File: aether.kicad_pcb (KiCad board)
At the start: 4 copper layers, 87 x 69.8 mm, 83 parts, among them J1 USB_C_Receptacle_USB2.0, J2 Conn_02x12_Top_Bottom, U1 CP2102N, U2 MCP73871_U, U3 LP2985-3.3, U4 LTC3525-5, U5 LoRa-E5

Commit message: Generated more 3d models for pcb
-
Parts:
- AE1: footprint Connector_Coaxial:SMA_Amphenol_132289_EdgeMount -> Connector_Coaxial:SMA_Amphenol_132134_Vertical
- J1: footprint Connector_USB:USB_C_Receptacle_Amphenol_12401610E4-2A -> Connector_USB:USB_C_Receptacle_XKB_U262-16XN-4BVC11
- moved Battery_Connect1 1.75 mm to (131.9, 136.0), turned to 180 degrees
- moved AE1 0.35 mm to (186.1, 94.0), turned to 90 degrees

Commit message: PCB edits
-
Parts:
- J2: value Conn_02x12_Top_Bottom -> Conn_01x05; footprint Connector_PinHeader_2.54mm:PinHeader_2x12_P2.54mm_Vertical -> Connector_PinHeader_1.27mm:PinHeader_1x05_P1.27mm_Vertical
- moved PMSensor1 49.9 mm to (184.8, 121.9), turned to -90 degrees
- moved R23 42.0 mm to (177.5, 123.8)
- moved R22 42.0 mm to (172.7, 123.8)
- moved J2 13.3 mm to (185.4, 91.4)
- moved AE1 13.1 mm to (182.9, 106.7)
- moved S1 12.3 mm to (174.6, 76.2)
- moved C14 12.0 mm to (153.9, 89.5)
- moved R21 6.87 mm to (148.6, 89.5)
- moved R20 6.79 mm to (148.6, 85.7)
- moved R19 6.06 mm to (154.0, 85.7)
- moved C2 4.45 mm to (123.2, 94.0)
- moved D1 4.44 mm to (122.6, 80.6)
- moved DC_InputTest1 4.44 mm to (121.9, 87.6)
- moved H3 3.42 mm to (184.8, 74.9)
- moved H1 3.18 mm to (184.8, 138.4)
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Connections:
- J2 pad 1: USB5V -> PA13/SWDIO
- J2 pad 2: +3.3V -> PA14/SWCLK
- J2 pad 3: PA13/SWDIO -> GND
- J2 pad 4: PA14/SWCLK -> RST
- J2 pad 5: RST -> unconnected-(J2-Pad5)
- U5 pad 24: PA13/SCK -> PB13/SCK
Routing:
- net GND: track 0.00 -> 2.19 mm
- net Net-(R15-Pad2): track 0.00 -> 0.97 mm
- added copper zone on In1.Cu, net +3.3V
- added copper zone on In2.Cu, net GND
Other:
- board size 87 x 69.8 mm -> 83.8 x 68.6 mm

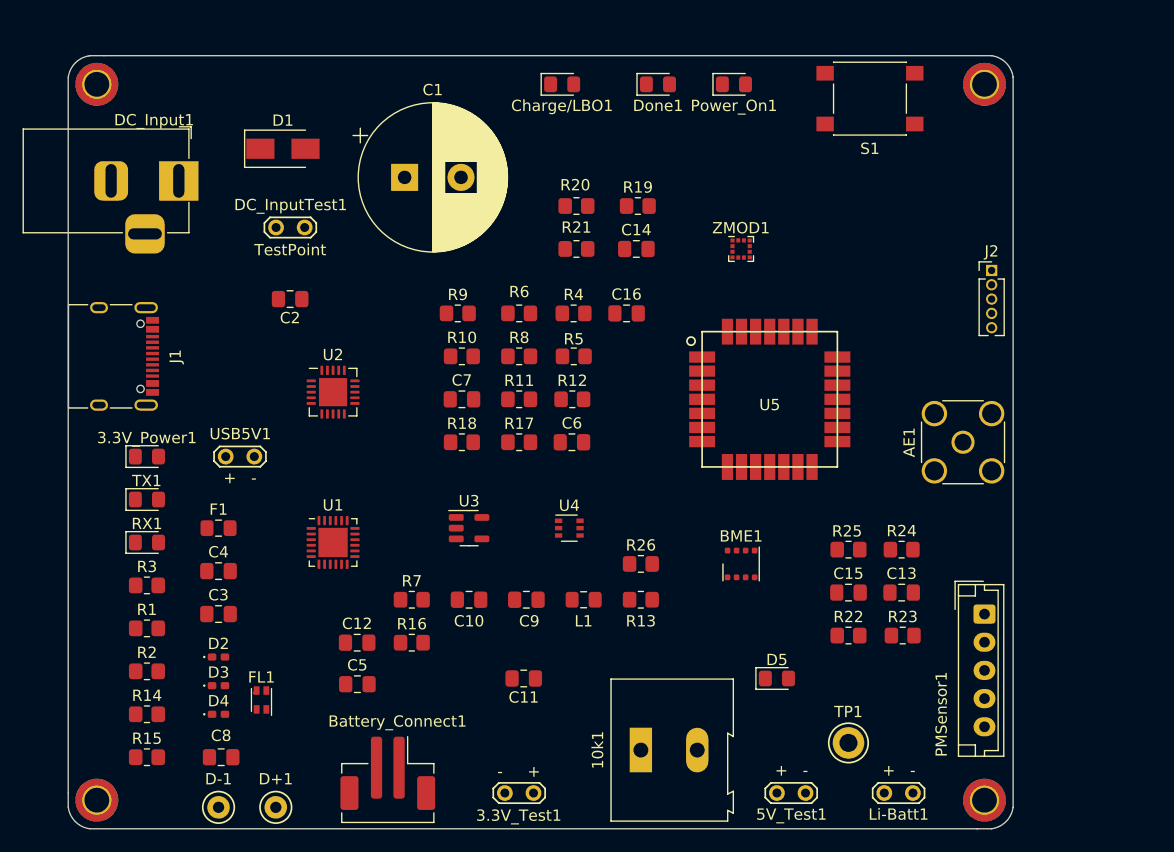
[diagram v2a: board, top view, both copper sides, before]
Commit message: Rearranged PCB for more efficient routing
-
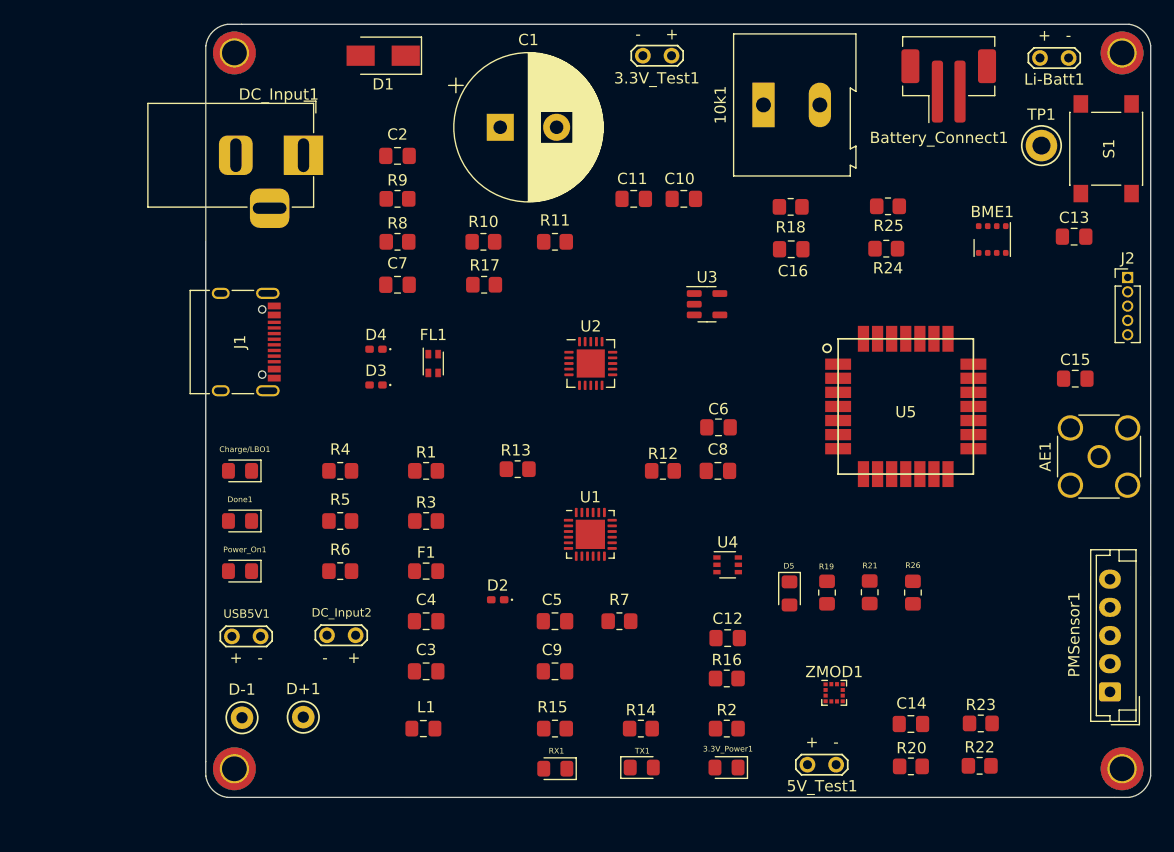
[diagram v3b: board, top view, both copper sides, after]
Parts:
- DC_Input2: renamed from DC_InputTest1; value TestPoint -> - +
- moved Battery_Connect1 78.7 mm to (181.6, 75.1), turned to 0 degrees
- moved Li-Batt1 66.6 mm to (189.7, 72.6)
- moved 3.3V_Test1 66.5 mm to (157.0, 72.4)
- moved Power_On1 61.5 mm to (118.7, 118.1), turned to 180 degrees
- moved 3.3V_Power1 58.3 mm to (161.9, 135.5), turned to 180 degrees
- moved 10k1 58.3 mm to (165.2, 76.8)
- moved R20 57.9 mm to (178.3, 135.4)
- moved TP1 55.7 mm to (189.8, 80.4)
- moved Done1 53.6 mm to (118.7, 113.7), turned to 180 degrees
- moved R2 51.7 mm to (161.9, 132.1)
- moved C8 50.9 mm to (161.1, 109.2), turned to 0 degrees
- moved TX1 49.9 mm to (154.4, 135.5)
- moved C14 48.7 mm to (178.3, 131.7), turned to 180 degrees
- moved Charge/LBO1 44.6 mm to (118.7, 109.2), turned to 180 degrees
- moved R14 43.8 mm to (154.3, 132.1)
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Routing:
- net GND: track 2.19 -> 0.00 mm
- net Net-(R15-Pad2): track 0.97 -> 0.00 mm

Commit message: PCB Routed
-
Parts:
- moved DC_Input2 53.5 mm to (154.3, 78.1)
- moved J2 31.1 mm to (197.4, 123.2)
- moved C7 21.3 mm to (153.7, 88.9)
- moved 5V_Test1 19.2 mm to (188.2, 134.6)
- moved PMSensor1 16.5 mm to (180.8, 135.4), turned to 180 degrees
- moved R1 15.3 mm to (130.8, 94.6), turned to 180 degrees
- moved R13 13.4 mm to (156.2, 113.0)
- moved R23 11.5 mm to (184.2, 120.1), turned to 90 degrees
- moved R20 10.5 mm to (184.9, 127.3), turned to 0 degrees
- moved R22 9.75 mm to (189.7, 127.3)
- moved C6 9.28 mm to (152.1, 107.4)
- moved R26 8.64 mm to (169.8, 120.1)
- moved C15 7.57 mm to (192.8, 93.5)
- moved D5 5.99 mm to (173.5, 120.1)
- moved R19 5.99 mm to (176.8, 120.0)
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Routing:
- net VCC: track 0.00 -> 181.9 mm, vias 0 -> 8
- net GND: track 0.00 -> 180.0 mm, vias 0 -> 58
- net Power On: track 0.00 -> 133.5 mm, vias 0 -> 2
- net Battery: track 0.00 -> 123.7 mm, vias 0 -> 8
- net PB15/SCL: track 0.00 -> 123.6 mm, vias 0 -> 6
- net PA15/SDA: track 0.00 -> 121.4 mm, vias 0 -> 6
- net Charge/LBO : track 0.00 -> 117.2 mm, vias 0 -> 3
- net Charge Done: track 0.00 -> 113.1 mm, vias 0 -> 3
- net RST: track 0.00 -> 110.4 mm, vias 0 -> 4
- net +3.3V: track 0.00 -> 75.1 mm, vias 0 -> 15
- net USB5V: track 0.00 -> 72.3 mm, vias 0 -> 3
- net PA14/SWCLK: track 0.00 -> 60.8 mm, vias 0 -> 1
- net Net-(L1-Pad2): track 0.00 -> 59.6 mm, vias 0 -> 2
- net Net-(D-1-Pad1): track 0.00 -> 58.5 mm, vias 0 -> 3
- net Net-(D+1-Pad1): track 0.00 -> 47.7 mm, vias 0 -> 1
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- added copper zone on F.Cu, net GND

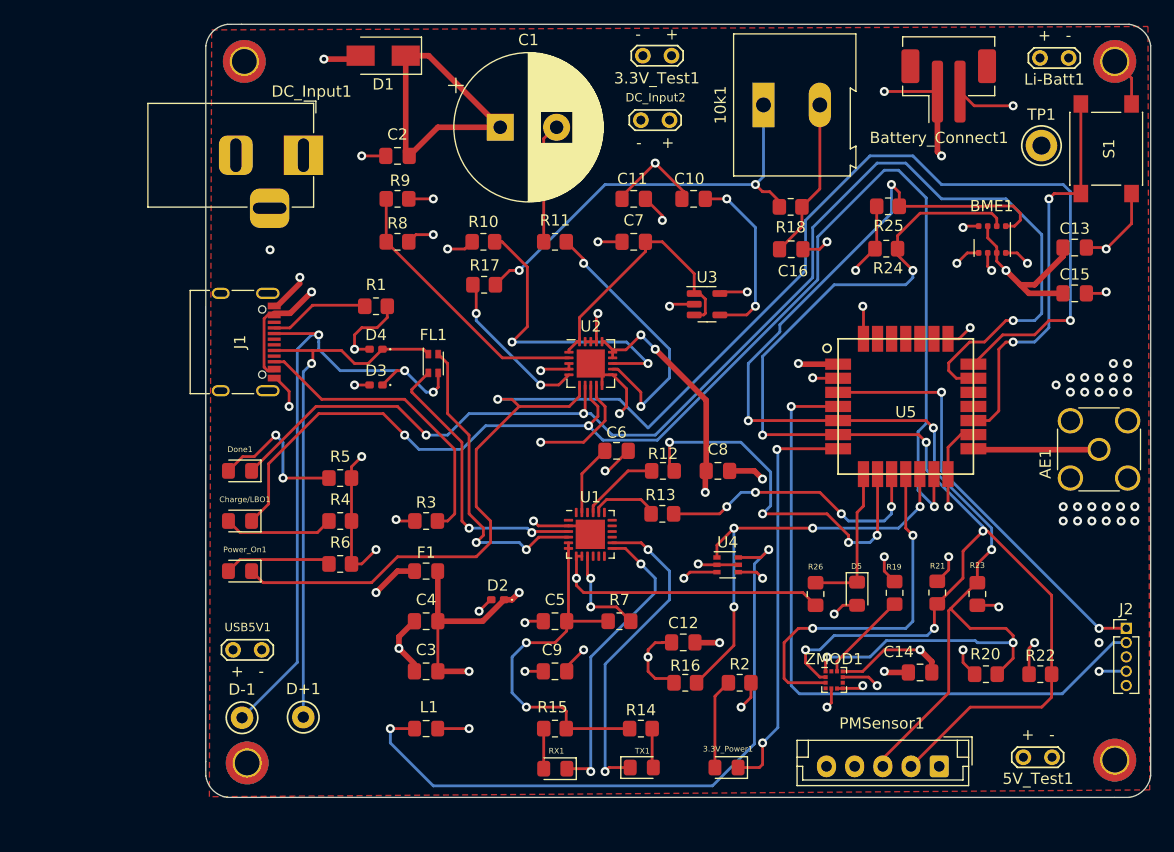
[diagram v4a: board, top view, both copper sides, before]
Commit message: DRC runs with 0 Errors. Updates connections and footprints.
-
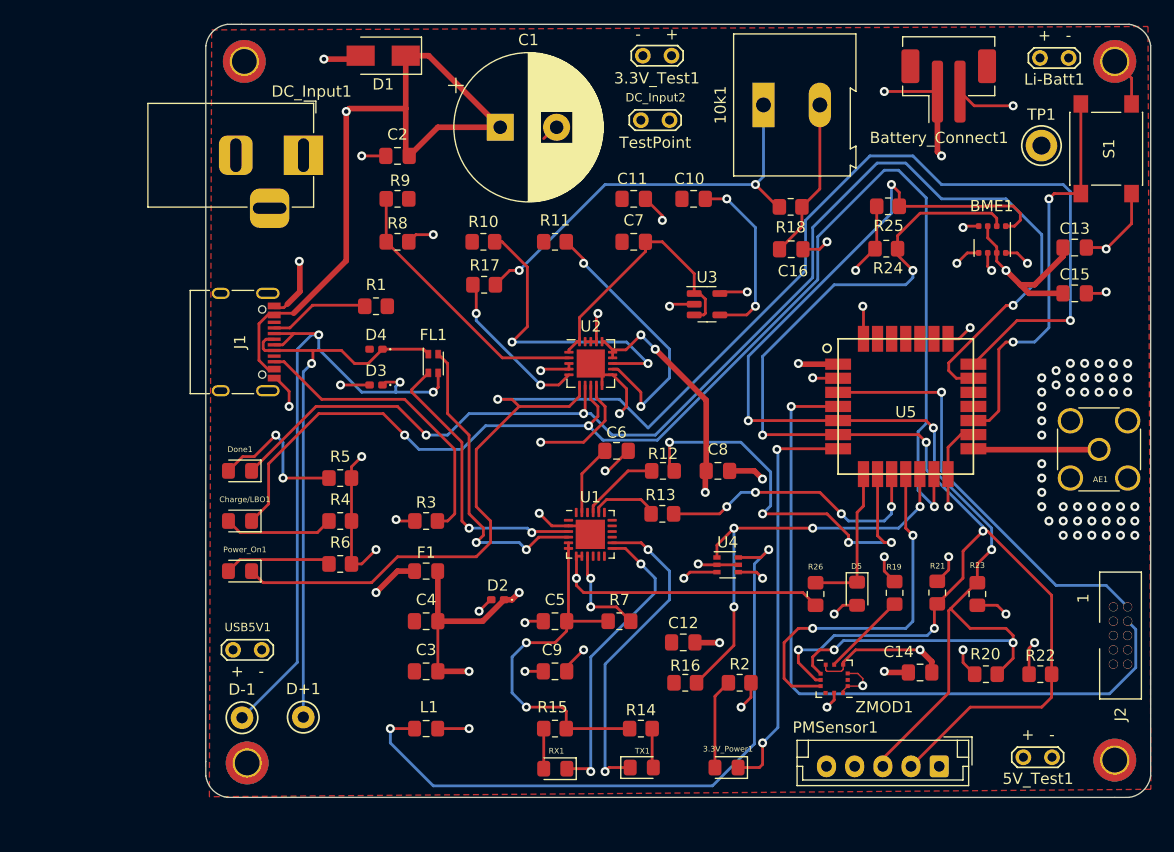
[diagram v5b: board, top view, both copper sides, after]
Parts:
- DC_Input2: value - + -> TestPoint
- J2: footprint Connector_PinHeader_1.27mm:PinHeader_1x05_P1.27mm_Vertical -> Aether:2X10_BOXHEADER
- ZMOD1: footprint Package_LGA:LGA-12_2x2mm_P0.5mm -> Aether:ZMOD4510
- moved J2 0.82 mm to (196.8, 123.8), turned to -90 degrees
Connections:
- J1 pad A6: unconnected-(J1-PadA6) -> Net-(D+1-Pad1)
- J1 pad A7: unconnected-(J1-PadA7) -> Net-(D-1-Pad1)
- J2 pad 1: PA13/SWDIO -> +3.3V
- J2 pad 2: PA14/SWCLK -> PA13/SWDIO
- J2 pad 4: RST -> PA14/SWCLK
- J2 pad 5: unconnected-(J2-Pad5) -> GND
- ZMOD1 pad 12: (no net) -> +3.3V
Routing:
- net GND: track 180.0 -> 117.1 mm, vias 58 -> 68
- net VCC: track 181.9 -> 198.3 mm
- net PA14/SWCLK: track 60.8 -> 65.2 mm
- net Net-(D+1-Pad1): track 47.7 -> 50.5 mm
- net +3.3V: track 75.1 -> 77.7 mm
- net Net-(D-1-Pad1): track 58.5 -> 60.9 mm
- net PB7/RX: track 34.1 -> 36.0 mm
- net Charge Done: track 113.1 -> 111.2 mm
- net /Power/GND_Break: track 39.8 -> 41.2 mm
- net RST: track 110.4 -> 111.7 mm, vias 4 -> 3
- net PB15/SCL: track 123.6 -> 124.5 mm
- net PA13/SWDIO: track 38.3 -> 37.7 mm, vias 2 -> 1
- net Net-(Power_On1-Pad2): track 9.50 -> 8.95 mm
- net Battery: track 123.7 -> 123.2 mm
- net Net-(R19-Pad2): track 8.10 -> 7.58 mm

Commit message: ZMOD Changes made
-
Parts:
- removed the C14 at (179.1, 127.1)
- removed the R20 at (184.9, 127.3)
- removed the R21 at (180.6, 120.0)
- removed the R22 at (189.7, 127.3)
- removed ZMOD1: Renesas, Aether:ZMOD4510
- added J2: ZMOD4510, Connector_JST:JST_XH_B4B-XH-A_1x04_P2.50mm_Vertical, F.Cu at (195.6, 87.0)
- added REF**: KiCad-Logo2_6mm_SilkScreen, Symbol:KiCad-Logo2_6mm_SilkScreen, B.Cu at (133.3, 132.7)
- moved S1 82.9 mm to (132.1, 134.0), turned to 180 degrees
- moved R20 15.1 mm to (170.2, 126.0), turned to -90 degrees
- moved L1 7.27 mm to (130.0, 127.0)
- moved R19 6.94 mm to (173.2, 126.0)
- moved C13 2.56 mm to (190.5, 88.3), turned to -90 degrees
- moved 5V_Test1 0.36 mm to (188.6, 134.6)
- renumbered C15 to C14, C16 to C15, J2 to J3, R23 to R20, R24 to R21, R25 to R22, R26 to R23
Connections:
- R19 pad 2: Net-(R19-Pad2) -> PA15/SDA
- U5 pad 11: PB5/ZMOD_INT -> PB5
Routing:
- net PA15/SDA: track 121.4 -> 89.1 mm, vias 6 -> 4
- net PB5/ZMOD_INT: track 32.2 -> 0.00 mm, vias 2 -> 0
- net PA3/RX2: track 0.00 -> 30.0 mm, vias 0 -> 1
- net PA2/TX2: track 0.00 -> 26.2 mm, vias 0 -> 1
- net +3.3V: track 77.7 -> 52.5 mm, vias 15 -> 10
- net RST: track 111.7 -> 133.0 mm
- net PB15/SCL: track 124.5 -> 108.1 mm, vias 6 -> 4
- net Net-(R19-Pad2): track 7.58 -> 0.00 mm
- net Battery: track 123.2 -> 129.7 mm
- net Net-(L1-Pad2): track 59.6 -> 62.3 mm
- net PA14/SWCLK: track 65.2 -> 67.2 mm
- net GND: track 117.1 -> 115.9 mm, vias 68 -> 66
